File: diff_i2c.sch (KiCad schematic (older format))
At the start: 16 parts, among them IC1 PCA9615DPJ, J4 SM07B-SRSS-TBLFSN

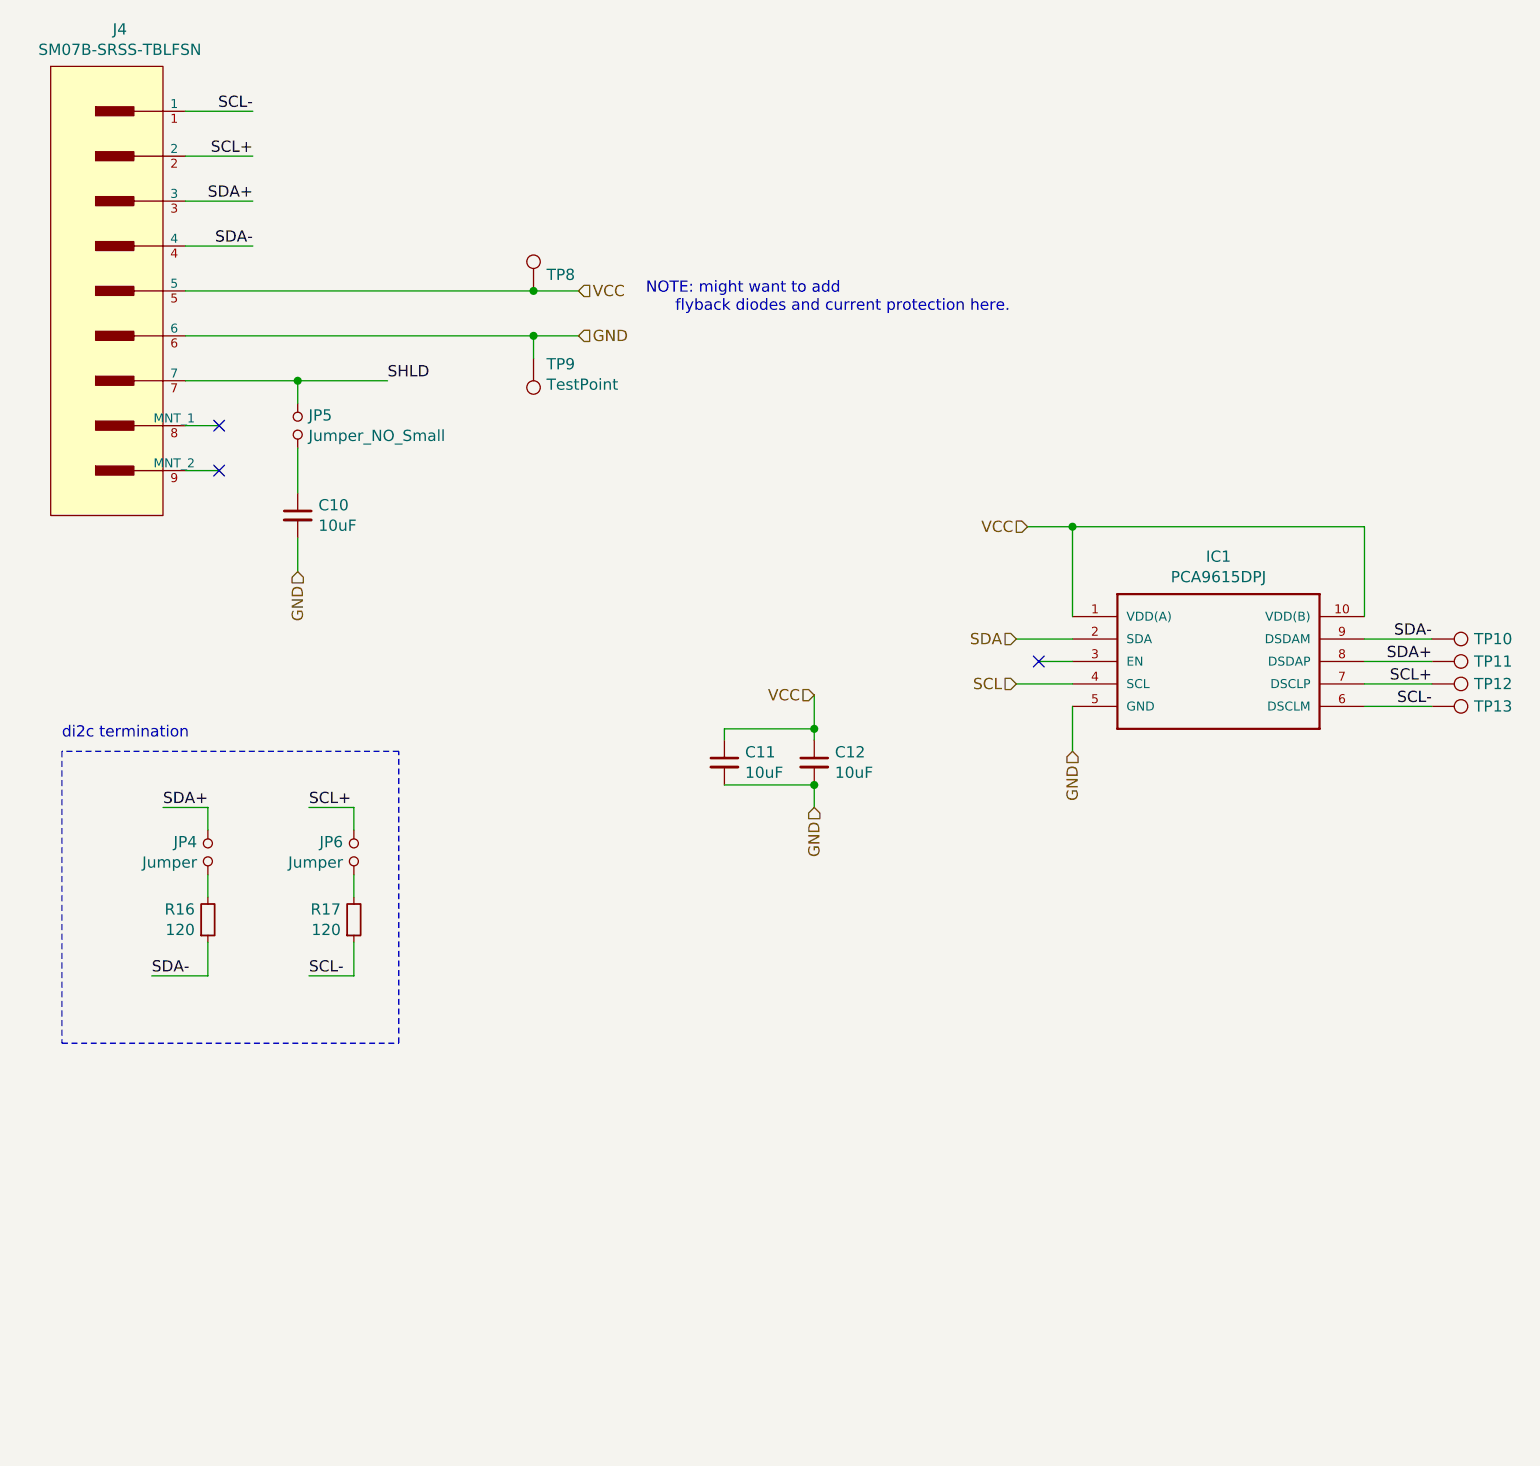
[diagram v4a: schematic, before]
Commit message: [rev.2 fixes]  - fix Q4 net pin assignment  - removed UVLO  - fix kelvin connection on R_sense  - fix MCP2515 symbol + pinout  - changed oscillator capacitors for 18uF load capacitance  - PCA9615 biasing resistors
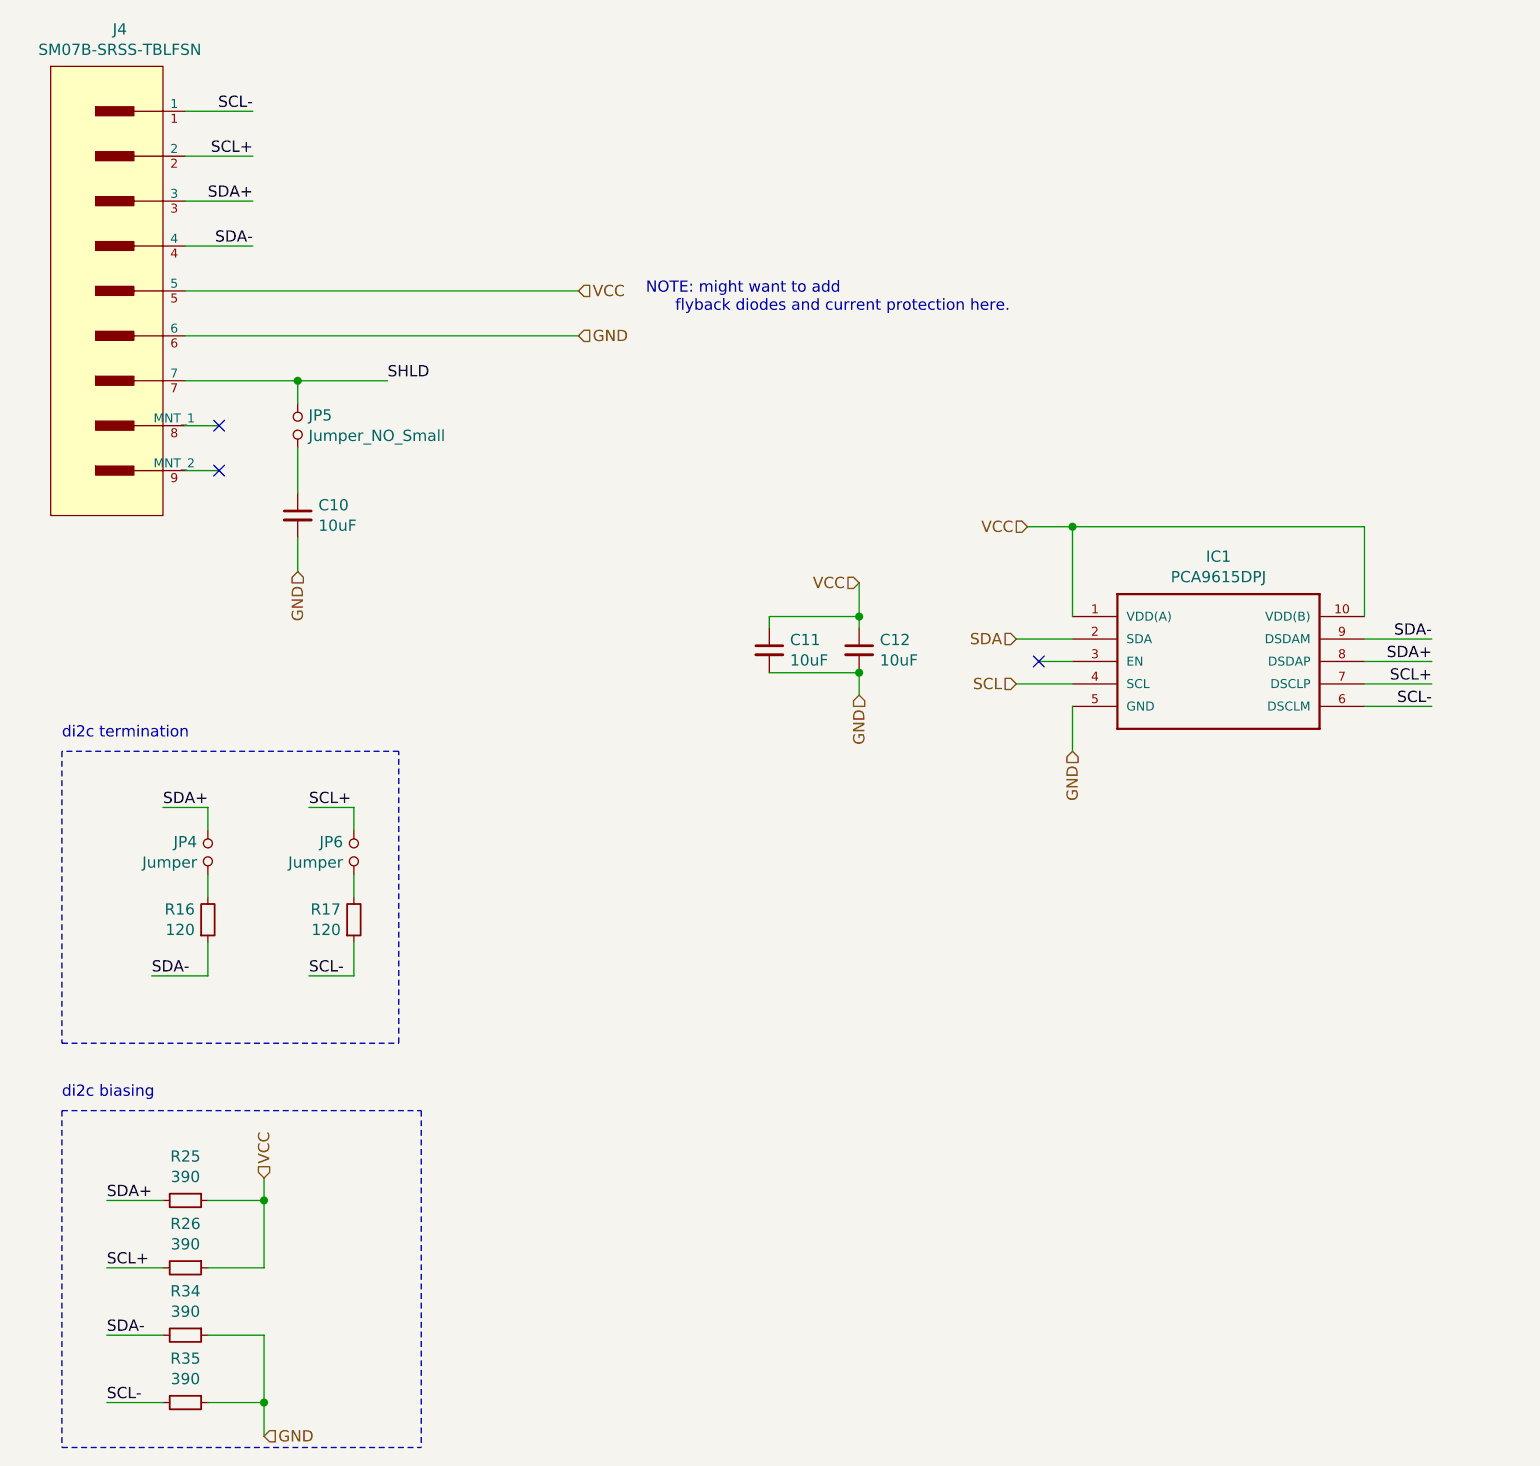
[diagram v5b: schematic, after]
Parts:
- removed TP10, TP11, TP12, TP13, TP8, TP9: TestPoint, TestPoint:TestPoint_Pad_D1.0mm, symbol Connector:TestPoint
- added R25, R26, R34, R35: 390, Resistor_SMD:R_0603_1608Metric_Pad1.05x0.95mm_HandSolder, symbol Device:R_Small
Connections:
- net GND: now also R34.1, R35.1
- net SCL+: now also R26.2
- net SCL-: now also R35.2
- net SDA+: now also R25.2
- net SDA-: now also R34.2
- net VCC: now also R25.1, R26.1
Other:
- note added: "di2c biasing\n"
- moved on the sheet: C11, C12
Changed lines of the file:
@@
 Text HLabel 5250 3150 0    50   Input ~ 0
 VCC
-Text HLabel 4300 4400 3    50   Input ~ 0
+Text HLabel 4500 3900 3    50   Input ~ 0
 GND
 Text HLabel 5200 3650 0    50   Input ~ 0
@@
 L Device:C_Small C12
 U 1 1 6198DB03
-P 4300 4200
-F 0 "C12" H 4392 4246 50  0000 L CNN
-F 1 "10uF" H 4392 4155 50  0000 L CNN
-F 2 "Capacitor_SMD:C_0603_1608Metric_Pad1.05x0.95mm_HandSolder" H 4300 4200 50  0001 C CNN
-F 3 "~" H 4300 4200 50  0001 C CNN
-F 4 "25V MLCC 10%" H 4300 4200 50  0001 C CNN "Description"
-F 5 "GRM188R61E106KA73J" H 4300 4200 50  0001 C CNN "Manufacturer_Part_Number"
-F 6 "EEPROM" H 4300 4200 50  0001 C CNN "category"
-F 7 "0603" H 4300 4200 50  0001 C CNN "package"
-	1    4300 4200
+P 4500 3700
+F 0 "C12" H 4592 3746 50  0000 L CNN
+F 1 "10uF" H 4592 3655 50  0000 L CNN
+F 2 "Capacitor_SMD:C_0603_1608Metric_Pad1.05x0.95mm_HandSolder" H 4500 3700 50  0001 C CNN
+F 3 "~" H 4500 3700 50  0001 C CNN
+F 4 "25V MLCC 10%" H 4500 3700 50  0001 C CNN "Description"
+F 5 "GRM188R61E106KA73J" H 4500 3700 50  0001 C CNN "Manufacturer_Part_Number"
+F 6 "EEPROM" H 4500 3700 50  0001 C CNN "category"
+F 7 "0603" H 4500 3700 50  0001 C CNN "package"
+	1    4500 3700
 	1    0    0    -1
 $EndComp
 Wire Wire Line
-	4300 4050 4300 4100
-Wire Wire Line
-	4300 4300 4300 4400
+	4500 3550 4500 3600
+Wire Wire Line
+	4500 3800 4500 3900
 $Comp
 L Device:C_Small C11
 U 1 1 61991791
-P 3900 4200
-F 0 "C11" H 3992 4246 50  0000 L CNN
-F 1 "10uF" H 3992 4155 50  0000 L CNN
-F 2 "Capacitor_SMD:C_0603_1608Metric_Pad1.05x0.95mm_HandSolder" H 3900 4200 50  0001 C CNN
-F 3 "~" H 3900 4200 50  0001 C CNN
-F 4 "25V MLCC 10%" H 3900 4200 50  0001 C CNN "Description"
-F 5 "GRM188R61E106KA73J" H 3900 4200 50  0001 C CNN "Manufacturer_Part_Number"
-F 6 "EEPROM" H 3900 4200 50  0001 C CNN "category"
-F 7 "0603" H 3900 4200 50  0001 C CNN "package"
-	1    3900 4200
+P 4100 3700
+F 0 "C11" H 4192 3746 50  0000 L CNN
+F 1 "10uF" H 4192 3655 50  0000 L CNN
+F 2 "Capacitor_SMD:C_0603_1608Metric_Pad1.05x0.95mm_HandSolder" H 4100 3700 50  0001 C CNN
+F 3 "~" H 4100 3700 50  0001 C CNN
+F 4 "25V MLCC 10%" H 4100 3700 50  0001 C CNN "Description"
+F 5 "GRM188R61E106KA73J" H 4100 3700 50  0001 C CNN "Manufacturer_Part_Number"
+F 6 "EEPROM" H 4100 3700 50  0001 C CNN "category"
+F 7 "0603" H 4100 3700 50  0001 C CNN "package"
+	1    4100 3700
 	1    0    0    -1
 $EndComp
 Wire Wire Line
-	3900 4050 3900 4100
-Wire Wire Line
-	3900 4050 4300 4050
-Wire Wire Line
-	4300 4300 3900 4300
-Connection ~ 4300 4300
+	4100 3550 4100 3600
+Wire Wire Line
+	4100 3550 4500 3550
+Wire Wire Line
+	4500 3800 4100 3800
+Connection ~ 4500 3800
 Wire Wire Line
 	6750 3950 7050 3950
@@
 Wire Wire Line
 	5450 4150 5450 3950
-Text HLabel 4300 3900 0    50   Input ~ 0
+Text HLabel 4500 3400 0    50   Input ~ 0
 VCC
 Wire Wire Line
-	4300 3900 4300 4050
-Connection ~ 4300 4050
+	4500 3400 4500 3550
+Connection ~ 4500 3550
 Wire Wire Line
 	5450 3150 6750 3150
@@
 Wire Wire Line
 	6750 3650 7050 3650
-$Comp
-L Connector:TestPoint TP10
-U 1 1 61B8A771
-P 7050 3650
-F 0 "TP10" V 7050 3838 50  0000 L CNN
-F 1 "TestPoint" V 7095 3838 50  0001 L CNN
-F 2 "TestPoint:TestPoint_Pad_D1.0mm" H 7250 3650 50  0001 C CNN
-F 3 "~" H 7250 3650 50  0001 C CNN
-	1    7050 3650
-	0    1    1    0
-$EndComp
-$Comp
-L Connector:TestPoint TP11
-U 1 1 61B8ADC9
-P 7050 3750
-F 0 "TP11" V 7050 3938 50  0000 L CNN
-F 1 "TestPoint" V 7095 3938 50  0001 L CNN
-F 2 "TestPoint:TestPoint_Pad_D1.0mm" H 7250 3750 50  0001 C CNN
-F 3 "~" H 7250 3750 50  0001 C CNN
-	1    7050 3750
-	0    1    1    0
-$EndComp
-$Comp
-L Connector:TestPoint TP12
-U 1 1 61B8C5BF
-P 7050 3850
-F 0 "TP12" V 7050 4038 50  0000 L CNN
-F 1 "TestPoint" V 7095 4038 50  0001 L CNN
-F 2 "TestPoint:TestPoint_Pad_D1.0mm" H 7250 3850 50  0001 C CNN
-F 3 "~" H 7250 3850 50  0001 C CNN
-	1    7050 3850
-	0    1    1    0
-$EndComp
-$Comp
-L Connector:TestPoint TP13
-U 1 1 61B8C5C5
-P 7050 3950
-F 0 "TP13" V 7050 4138 50  0000 L CNN
-F 1 "TestPoint" V 7095 4138 50  0001 L CNN
-F 2 "TestPoint:TestPoint_Pad_D1.0mm" H 7250 3950 50  0001 C CNN
-F 3 "~" H 7250 3950 50  0001 C CNN
-	1    7050 3950
-	0    1    1    0
-$EndComp
-Wire Wire Line
-	1500 2100 3050 2100
-Wire Wire Line
-	1500 2300 3050 2300
-$Comp
-L Connector:TestPoint TP9
-U 1 1 61B915B9
-P 3050 2400
-F 0 "TP9" H 2992 2426 50  0000 R CNN
-F 1 "TestPoint" H 2992 2517 50  0000 R CNN
-F 2 "TestPoint:TestPoint_Pad_D1.0mm" H 3250 2400 50  0001 C CNN
-F 3 "~" H 3250 2400 50  0001 C CNN
-	1    3050 2400
-	-1   0    0    1
-$EndComp
-Wire Wire Line
-	3050 2400 3050 2300
-Connection ~ 3050 2300
-Wire Wire Line
-	3050 2300 3250 2300
-$Comp
-L Connector:TestPoint TP8
-U 1 1 61B932FB
-P 3050 2100
-F 0 "TP8" H 3108 2172 50  0000 L CNN
-F 1 "TestPoint" H 3108 2127 50  0001 L CNN
-F 2 "TestPoint:TestPoint_Pad_D1.0mm" H 3250 2100 50  0001 C CNN
-F 3 "~" H 3250 2100 50  0001 C CNN
-	1    3050 2100
-	1    0    0    -1
-$EndComp
-Connection ~ 3050 2100
-Wire Wire Line
-	3050 2100 3250 2100
+Text Label 1150 6150 0    50   ~ 0
+SDA+
+Wire Wire Line
+	1150 6150 1400 6150
+$Comp
+L Device:R_Small R25
+U 1 1 61E38411
+P 1500 6150
+F 0 "R25" V 1304 6150 50  0000 C CNN
+F 1 "390" V 1395 6150 50  0000 C CNN
+F 2 "Resistor_SMD:R_0603_1608Metric_Pad1.05x0.95mm_HandSolder" H 1500 6150 50  0001 C CNN
+F 3 "~" H 1500 6150 50  0001 C CNN
+	1    1500 6150
+	0    1    1    0
+$EndComp
+Text Label 1150 6450 0    50   ~ 0
+SCL+
+Wire Wire Line
+	1150 6450 1400 6450
+$Comp
+L Device:R_Small R26
+U 1 1 61E38A1C
+P 1500 6450
+F 0 "R26" V 1304 6450 50  0000 C CNN
+F 1 "390" V 1395 6450 50  0000 C CNN
+F 2 "Resistor_SMD:R_0603_1608Metric_Pad1.05x0.95mm_HandSolder" H 1500 6450 50  0001 C CNN
+F 3 "~" H 1500 6450 50  0001 C CNN
+	1    1500 6450
+	0    1    1    0
+$EndComp
+Text Label 1150 6750 0    50   ~ 0
+SDA-
+Wire Wire Line
+	1150 6750 1400 6750
+$Comp
+L Device:R_Small R34
+U 1 1 61E3A364
+P 1500 6750
+F 0 "R34" V 1304 6750 50  0000 C CNN
+F 1 "390" V 1395 6750 50  0000 C CNN
+F 2 "Resistor_SMD:R_0603_1608Metric_Pad1.05x0.95mm_HandSolder" H 1500 6750 50  0001 C CNN
+F 3 "~" H 1500 6750 50  0001 C CNN
+	1    1500 6750
+	0    1    1    0
+$EndComp
+Text Label 1150 7050 0    50   ~ 0
+SCL-
+Wire Wire Line
+	1150 7050 1400 7050
+$Comp
+L Device:R_Small R35
+U 1 1 61E3A36C
+P 1500 7050
+F 0 "R35" V 1304 7050 50  0000 C CNN
+F 1 "390" V 1395 7050 50  0000 C CNN
+F 2 "Resistor_SMD:R_0603_1608Metric_Pad1.05x0.95mm_HandSolder" H 1500 7050 50  0001 C CNN
+F 3 "~" H 1500 7050 50  0001 C CNN
+	1    1500 7050
+	0    1    1    0
+$EndComp
+Wire Wire Line
+	1600 6450 1850 6450
+Wire Wire Line
+	1850 6450 1850 6150
+Wire Wire Line
+	1600 6150 1850 6150
+Connection ~ 1850 6150
+Wire Wire Line
+	1850 6150 1850 6050
+Text HLabel 1850 6050 1    50   Input ~ 0
+VCC
+Wire Wire Line
+	1600 6750 1850 6750
+Wire Wire Line
+	1850 6750 1850 7050
+Wire Wire Line
+	1600 7050 1850 7050
+Connection ~ 1850 7050
+Wire Wire Line
+	1850 7050 1850 7200
+Text HLabel 1850 7200 2    50   Input ~ 0
+GND
+Wire Wire Line
+	1500 2300 3250 2300
+Wire Wire Line
+	1500 2100 3250 2100
+Text Notes 950  5700 0    50   ~ 0
+di2c biasing\n
+Wire Notes Line
+	2550 5750 2550 7250
+Wire Notes Line
+	950  5750 2550 5750
+Wire Notes Line
+	950  5750 950  7250
+Wire Notes Line
+	950  7250 2550 7250
 $EndSCHEMATC
